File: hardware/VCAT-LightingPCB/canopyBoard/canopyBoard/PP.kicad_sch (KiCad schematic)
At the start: 18 parts, among them IC1 LM74502DDFR, Q1 PSMN012-100YS, Q2 PSMN012-100YS

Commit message: pray for no errors, more stuff to add
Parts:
- renumbered C4 to C10, C5 to C11, C6 to C12, C7 to C13, C1 to C7, C2 to C8, C3 to C9, D2 to D1, D1 to D2, R1 to R3, R2 to R4, R3 to R5, R4 to R6, R5 to R7, R6 to R8

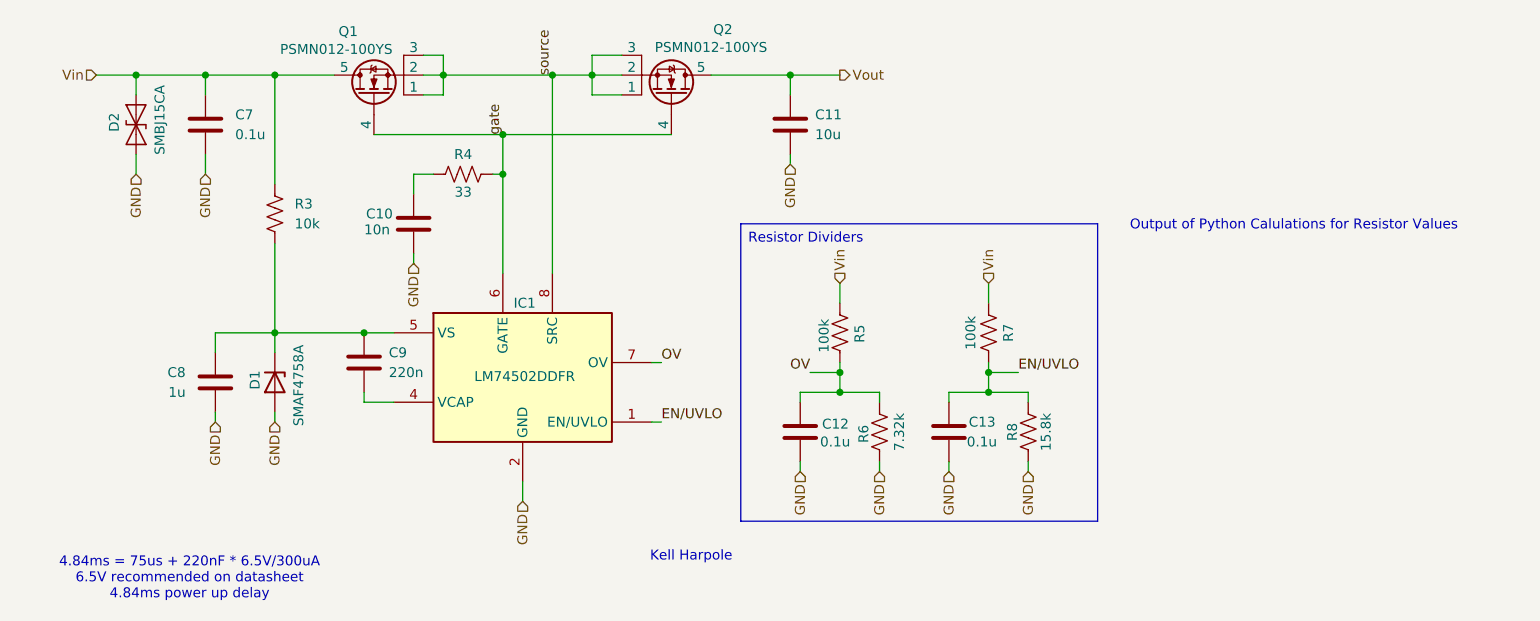
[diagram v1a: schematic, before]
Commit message: Untrack KiCad .history, convert KiCAD-Sharepoint to a submodule, remove LightsPCB
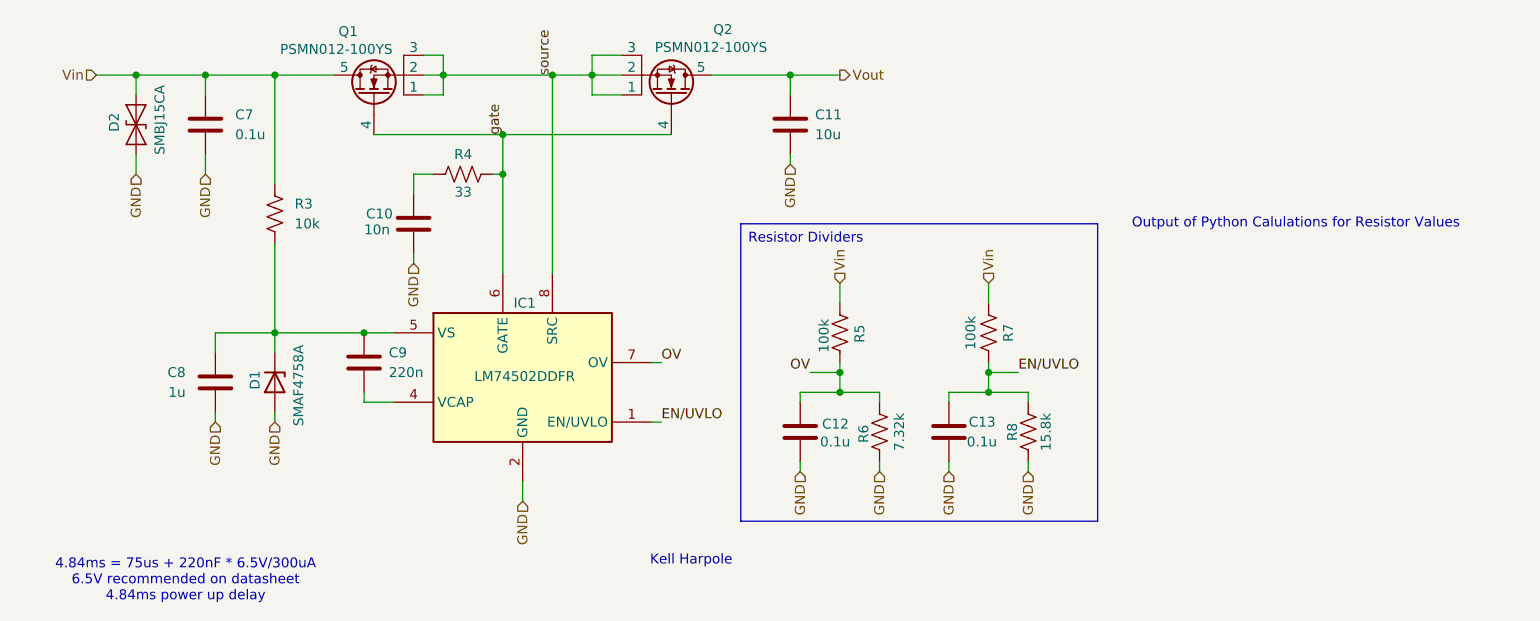
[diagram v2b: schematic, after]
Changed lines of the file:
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@@
 	(text "4.84ms = 75us + 220nF * 6.5V/300uA\n6.5V recommended on datasheet\n4.84ms power up delay"
 		(exclude_from_sim no)
-		(at 32.258 108.966 0)
+		(at 31.75 109.22 0)
 		(effects
 			(font
@@
 	(text "Output of Python Calulations for Resistor Values"
 		(exclude_from_sim no)
-		(at 173.736 63.754 0)
+		(at 173.99 63.5 0)
 		(effects
 			(font
@@
 	(text "Kell Harpole"
 		(exclude_from_sim no)
-		(at 96.52 106.172 0)
+		(at 96.52 106.68 0)
 		(effects
 			(font
